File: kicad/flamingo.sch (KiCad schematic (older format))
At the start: 45 parts, among them J1 SWD, J2 Conn_01x02, J3 Conn_01x02, J4 Conn_01x03, J5 Conn_01x02, Q0 Q_PMOS_GSD, Q1 Q_PMOS_GSD, Q2 Q_PMOS_GSD, SW0 SW, SW1 SW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

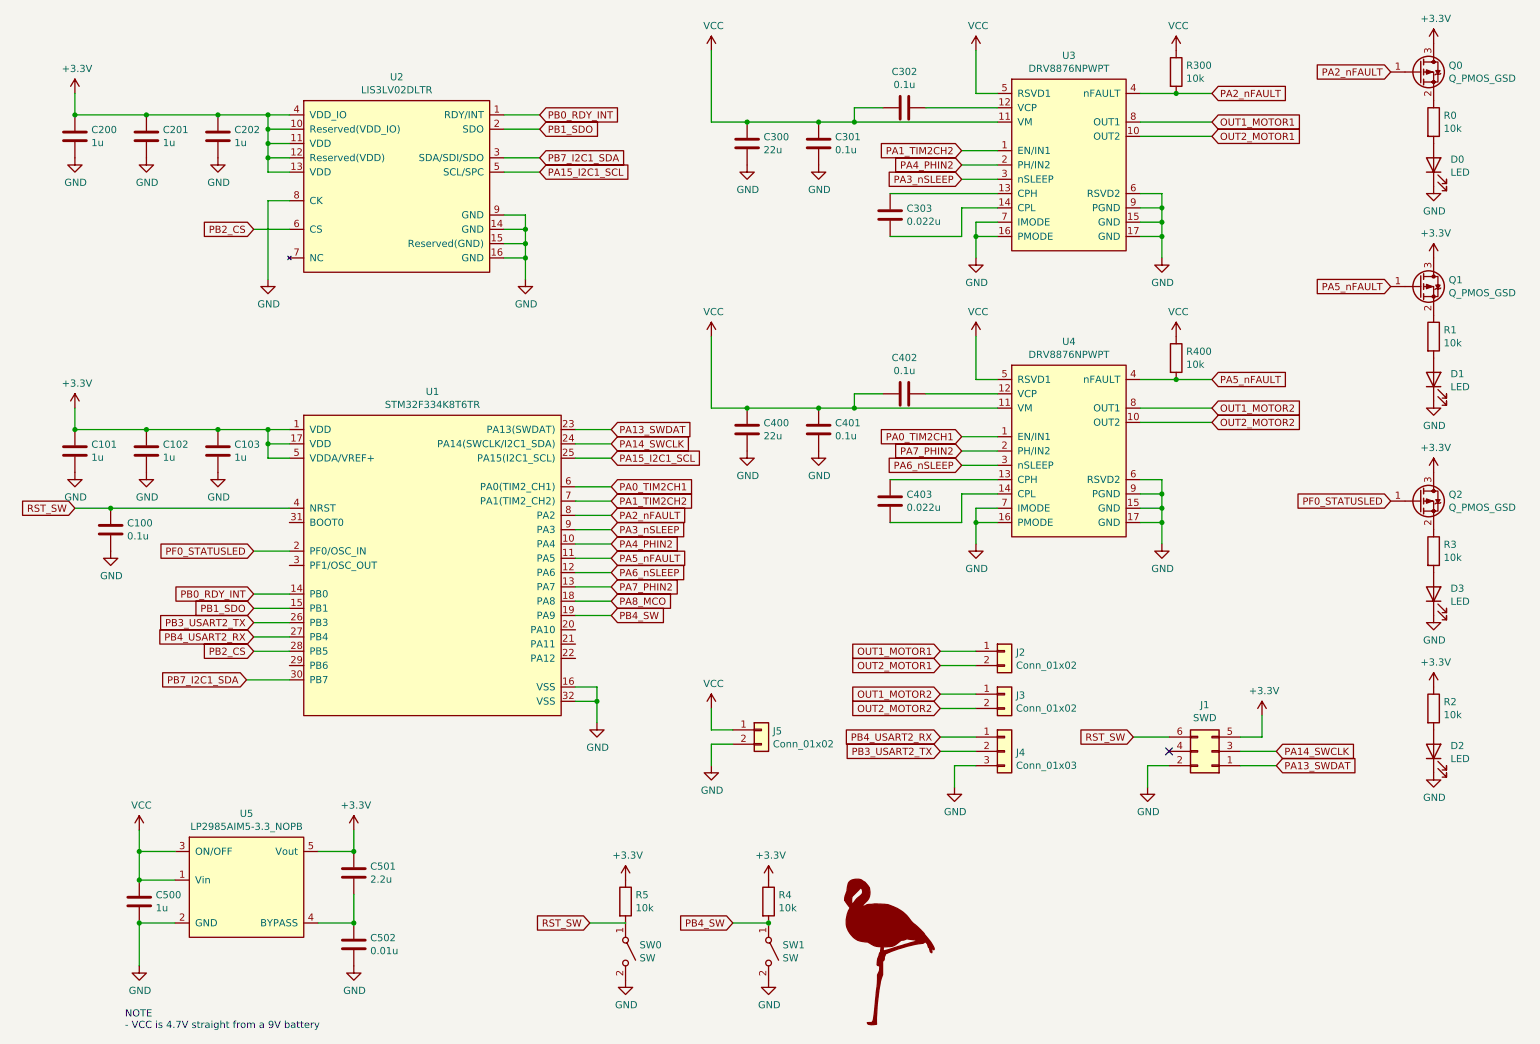
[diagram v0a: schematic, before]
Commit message: Revision 2
Changed the following items on the schematic and layout.
 - Disconnected SDO from U1 and U2
 - Changed U3 and U4 pull up resistors to have a source of 3.3V, not VCC
 - Added 1k I2C resistors
 - Fixed U5 BYPASS connection error
 - Updated schematic photo
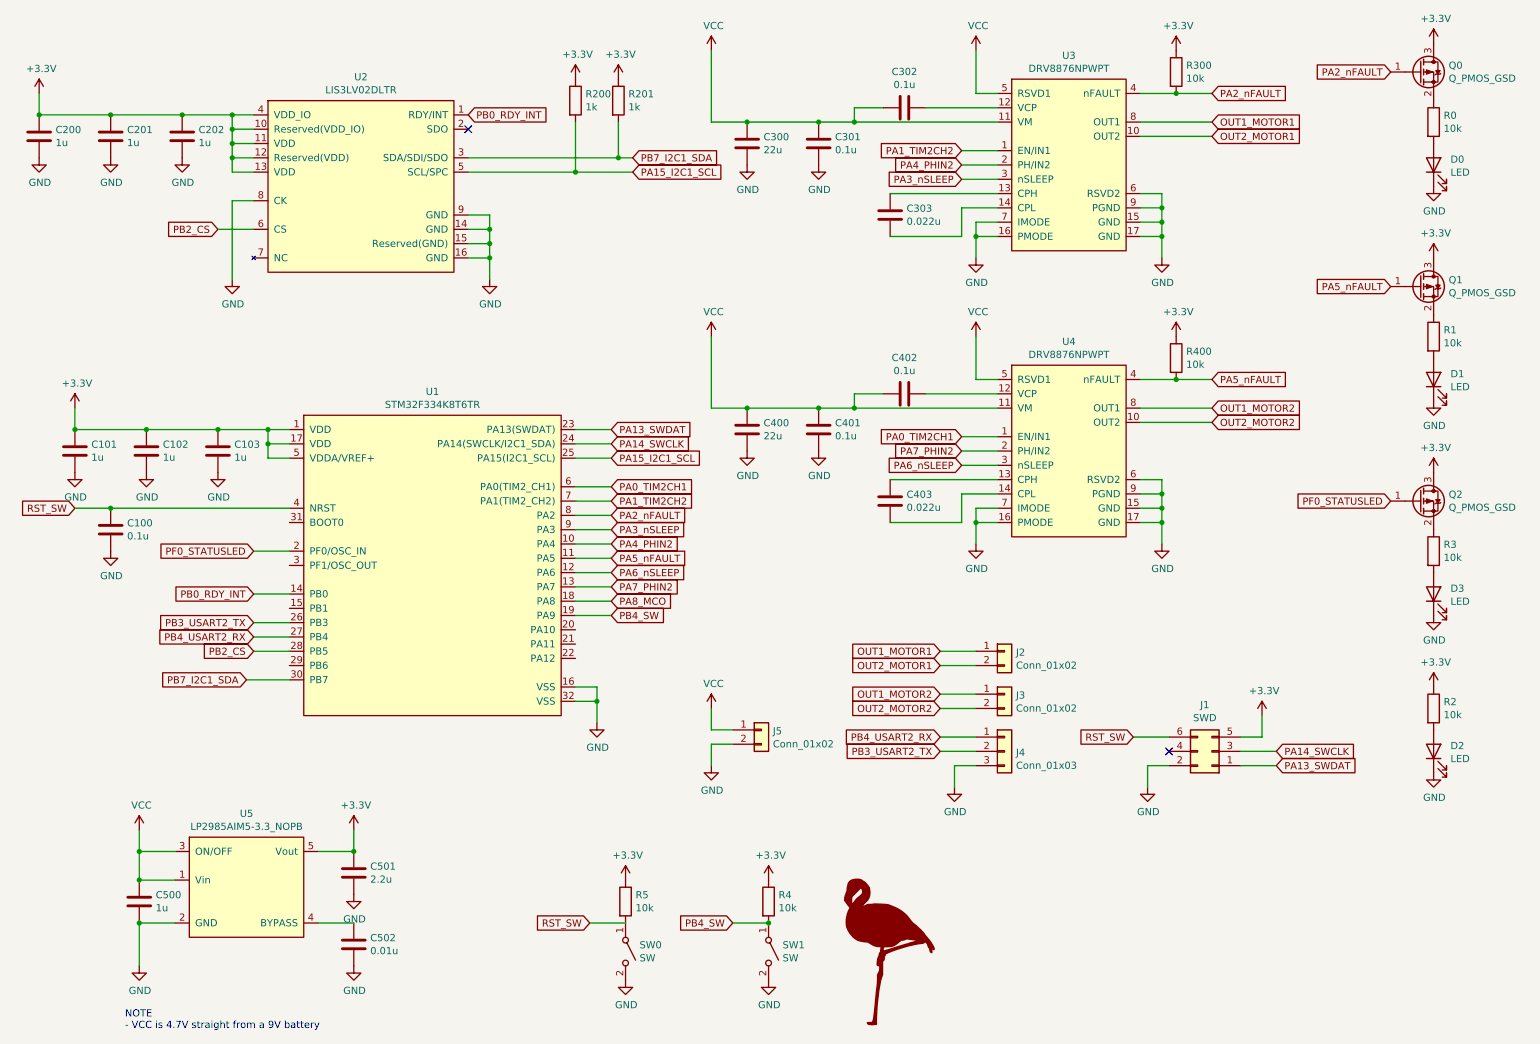
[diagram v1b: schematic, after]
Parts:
- added R200, R201: 1k, Resistor_SMD:R_0603_1608Metric_Pad0.98x0.95mm_HandSolder, symbol Device:R
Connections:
- net +3V3: now also R300.1, R400.1, R200.1, R201.1
- net GND: now also C501.2
- net PA15_I2C1_SCL: now also R200.2
- net PB7_I2C1_SDA: now also R201.2
- net VCC: no longer R300.1, R400.1
- net at C502.1, U5.4 (BYPASS): no longer C501.2
- net PB1_SDO: no longer names the net of U1.15 (PB1)
- net PB1_SDO: no longer U2.2 (SDO)
- no-connect marks 1 -> 2
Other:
- moved on the sheet: C200, C201, C202, U2
